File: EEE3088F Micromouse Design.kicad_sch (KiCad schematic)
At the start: 42 parts, among them J1 Conn_02x16_Odd_Even, J2 Conn_01x02, U1 INA219AxD, U2 DRV8837, U3 DRV8837, U4 DRV8837, U5 DRV8837, U6 TPS5430DDA, U7 TPS61088RHLR

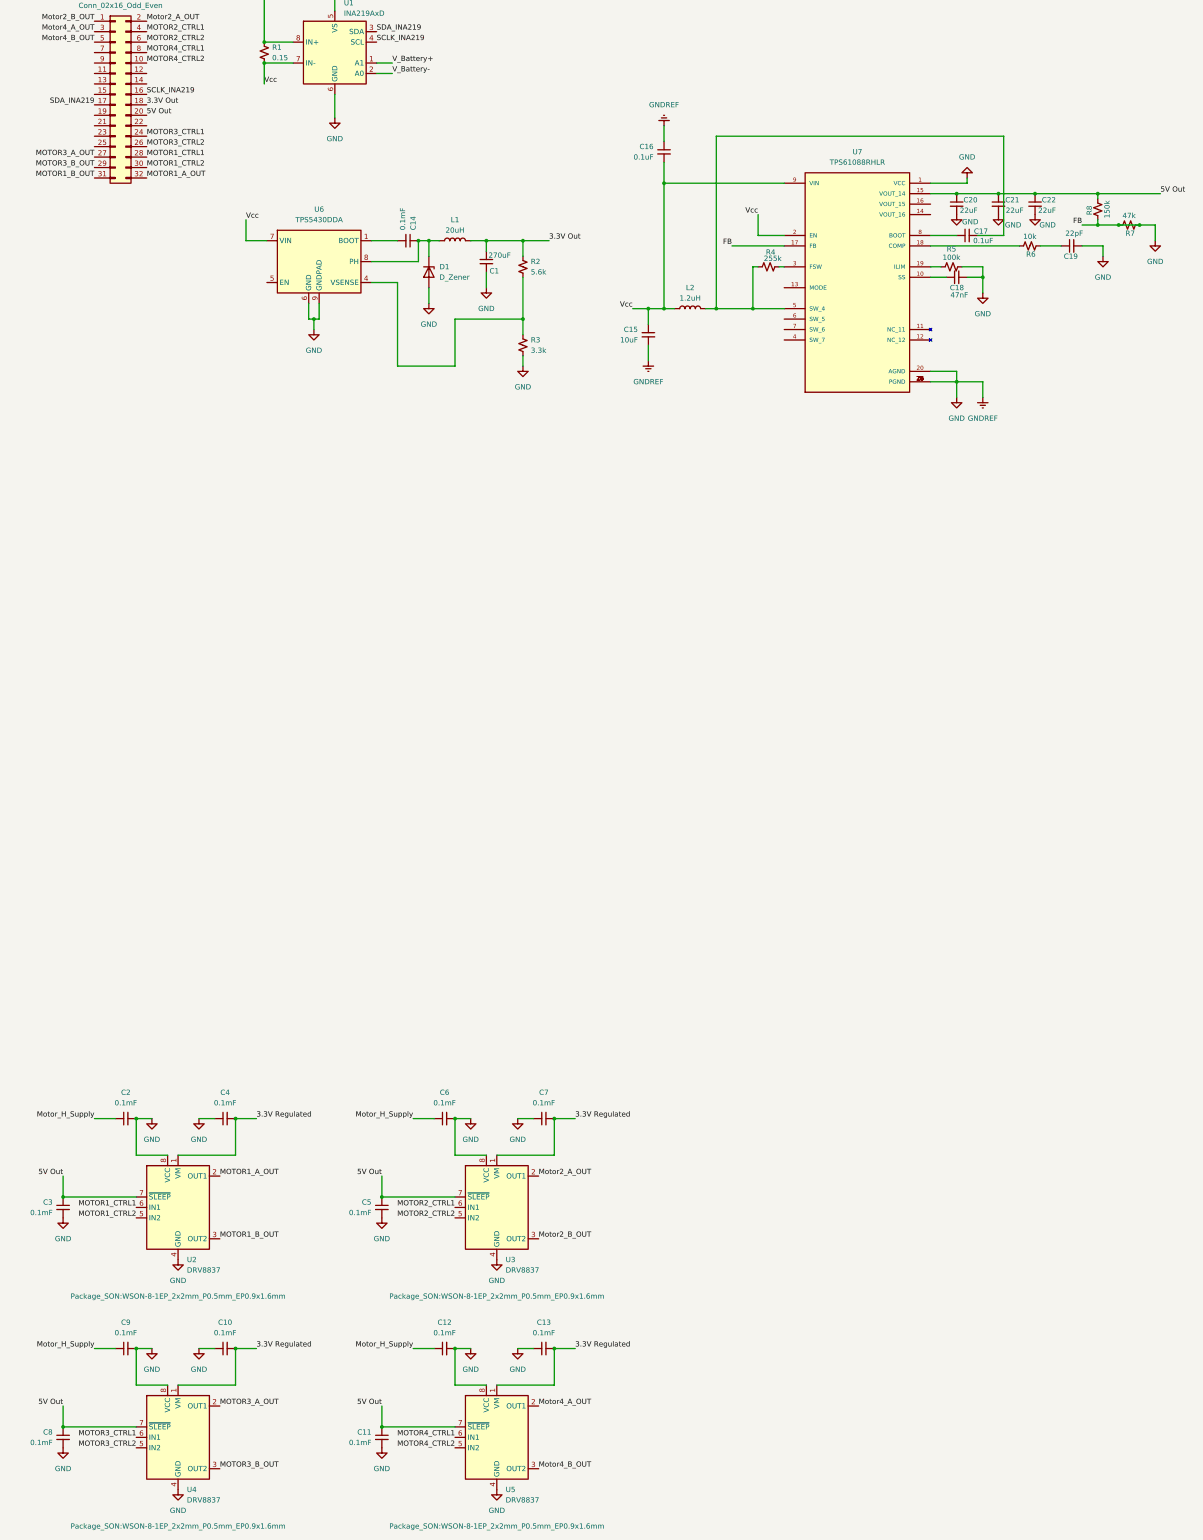
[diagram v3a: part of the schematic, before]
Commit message: Added the Battery Charging Circuit
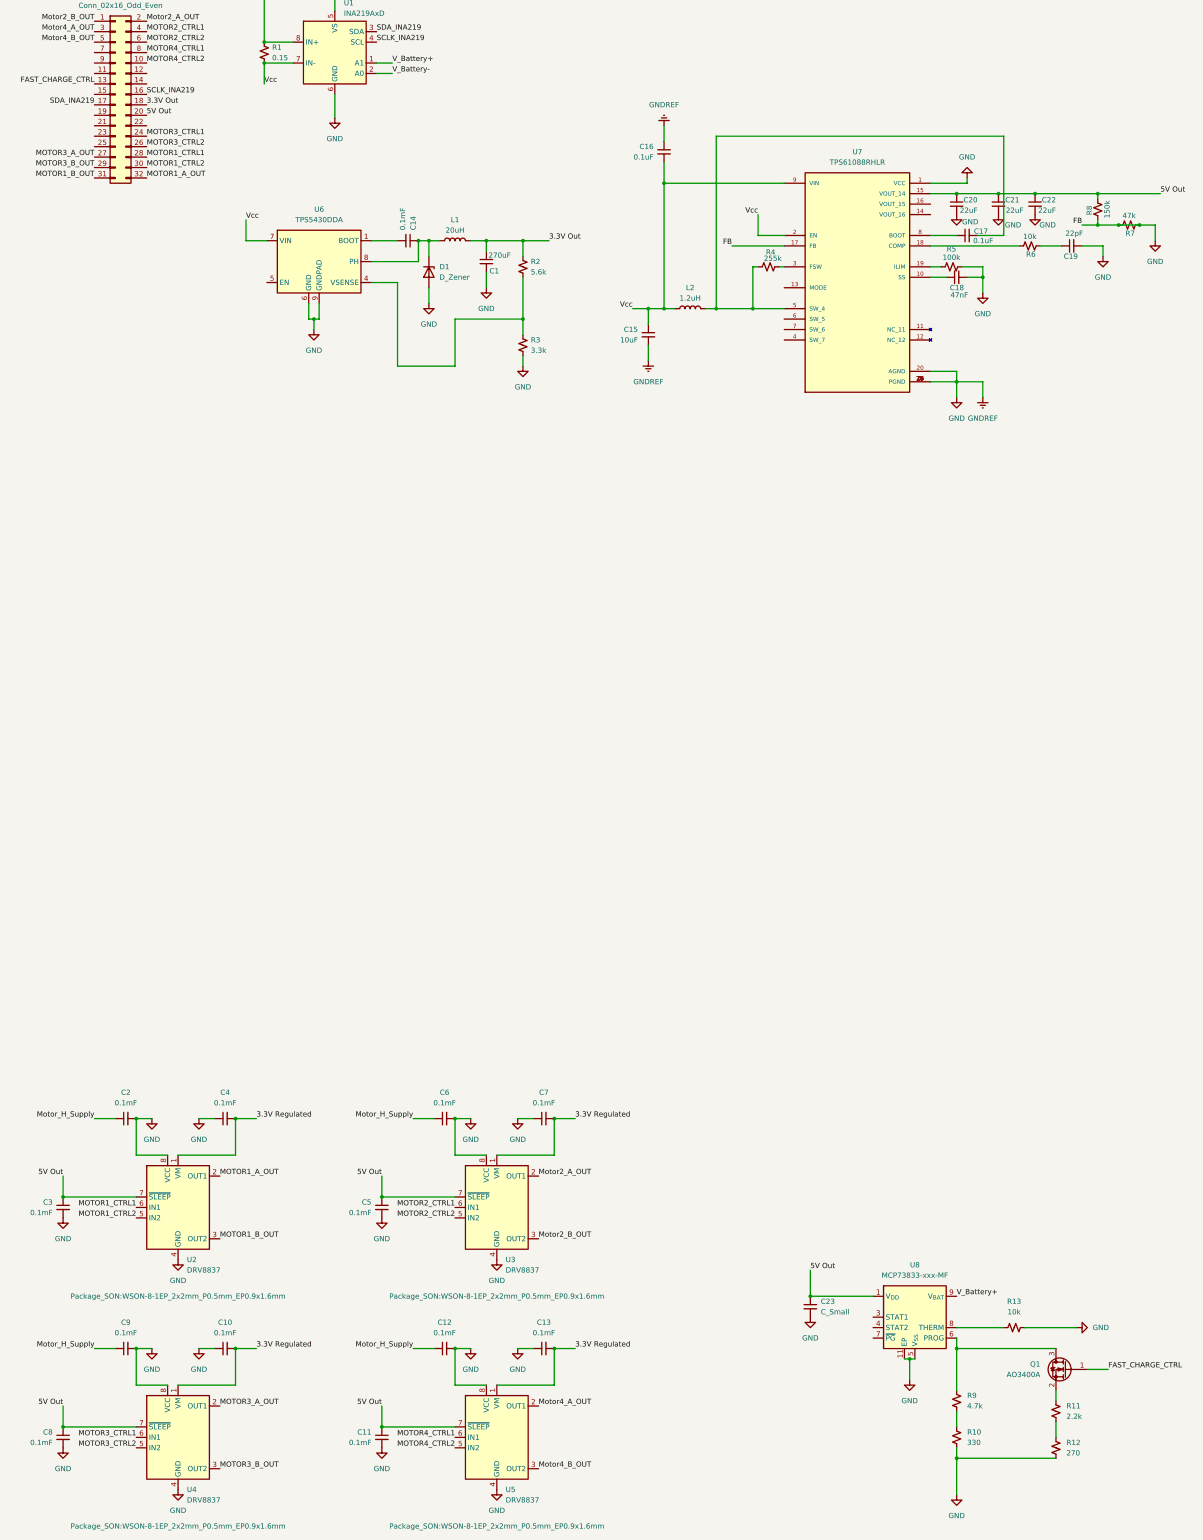
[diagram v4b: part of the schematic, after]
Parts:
- added C23: C_Small, symbol Device:C_Small
- added Q1: AO3400A, Package_TO_SOT_SMD:SOT-23, symbol Transistor_FET:AO3400A
- added R10: 330, Resistor_SMD:R_1206_3216Metric_Pad1.30x1.75mm_HandSolder, symbol Device:R_Small_US
- added R11: 2.2k, Resistor_SMD:R_1206_3216Metric_Pad1.30x1.75mm_HandSolder, symbol Device:R_Small_US
- added R12: 270, Resistor_SMD:R_1206_3216Metric_Pad1.30x1.75mm_HandSolder, symbol Device:R_Small_US
- added R13: 10k, Resistor_SMD:R_1206_3216Metric_Pad1.30x1.75mm_HandSolder, symbol Device:R_Small_US
- added R9: 4.7k, Resistor_SMD:R_1206_3216Metric_Pad1.30x1.75mm_HandSolder, symbol Device:R_Small_US
- added U8: MCP73833-xxx-MF, Package_DFN_QFN:DFN-10-1EP_3x3mm_P0.5mm_EP1.58x2.35mm, symbol Battery_Management:MCP73833-xxx-MF
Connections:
- net 5V Out: now also C23.1, U8.1 (V_{DD}), U8.2 (V_{DD})
- net GND: now also C23.2, R10.2, R12.2, R13.2, U8.11 (EP), U8.5 (V_{SS})
- net V_Battery+: now also U8.10 (V_{BAT}), U8.9 (V_{BAT})
- net FAST_CHARGE_CTRL: now reaches J1.13 (Pin_13)
- net FAST_CHARGE_CTRL: now also Q1.1 (G)
- new net: Q1.3 (D), R9.1, U8.6 (PROG)
- new net: R13.1, U8.8 (THERM)
- new net: Q1.2 (S), R11.1
- new net: R10.1, R9.2
- new net: R11.2, R12.1

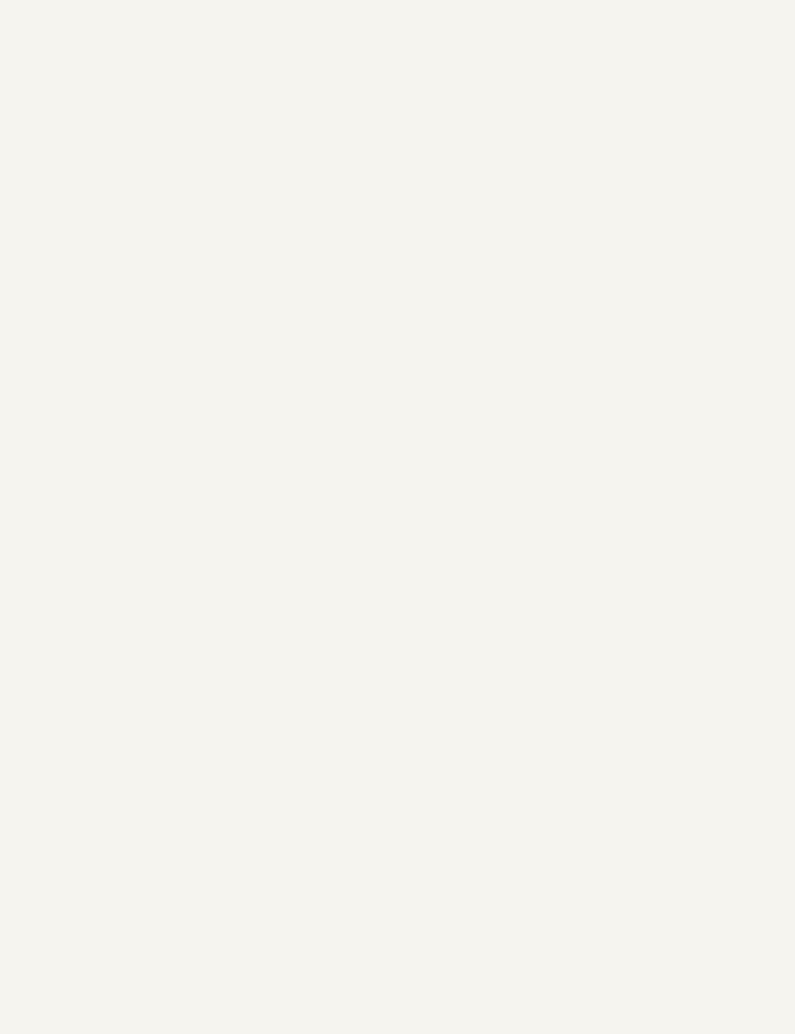
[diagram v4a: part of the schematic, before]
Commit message: Added Type-C 9V integration
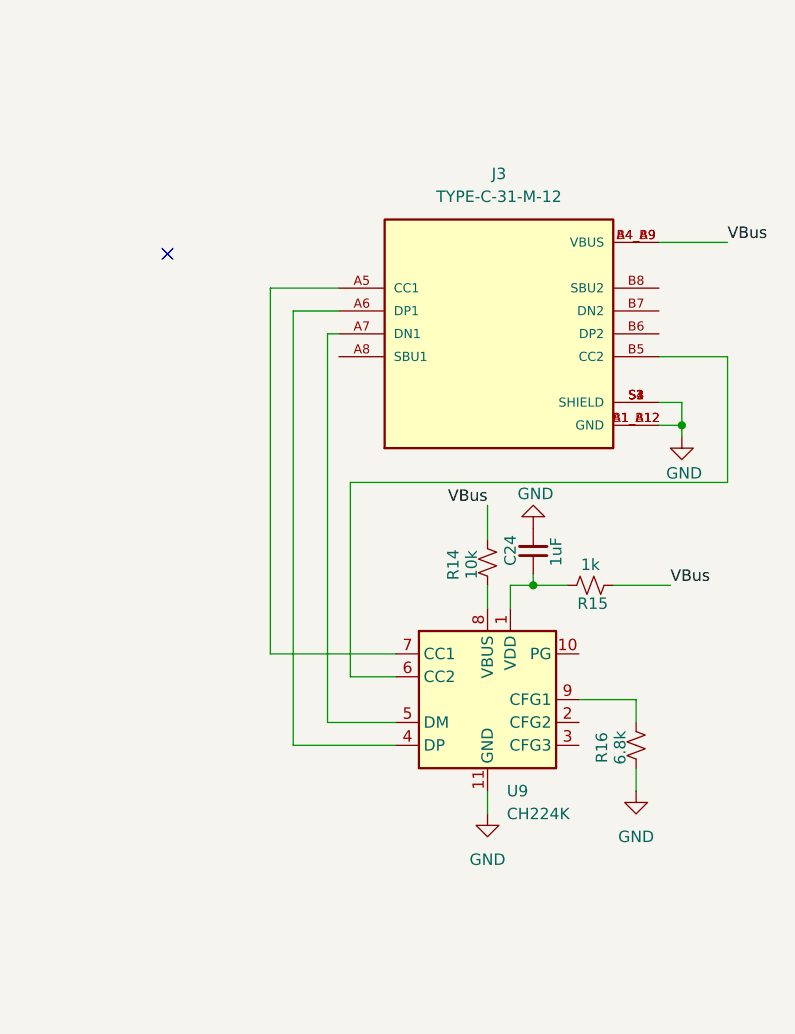
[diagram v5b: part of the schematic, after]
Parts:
- added C24: 1uF, Capacitor_SMD:C_0402_1005Metric_Pad0.74x0.62mm_HandSolder, symbol Device:C_Small
- added J3: TYPE-C-31-M-12, TYPE-C-31-M-12:HRO_TYPE-C-31-M-12, symbol TYPE-C-31-M-12:TYPE-C-31-M-12
- added R14: 10k, Resistor_SMD:R_1206_3216Metric_Pad1.30x1.75mm_HandSolder, symbol Device:R_Small_US
- added R15: 1k, Resistor_SMD:R_1206_3216Metric_Pad1.30x1.75mm_HandSolder, symbol Device:R_Small_US
- added R16: 6.8k, Resistor_SMD:R_1206_3216Metric_Pad1.30x1.75mm_HandSolder, symbol Device:R_Small_US
- added U9: CH224K, Package_SO:SSOP-10-1EP_3.9x4.9mm_P1mm_EP2.1x3.3mm, symbol Interface_USB:CH224K
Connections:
- net GND: now also C24.2, J3.A1_B12 (GND), J3.B1_A12 (GND), J3.S1 (SHIELD), J3.S2 (SHIELD), J3.S3 (SHIELD), J3.S4 (SHIELD), R16.1, U9.11 (GND)
- new net: R14.1, U9.8 (VBUS)
- new net: C24.1, R15.2, U9.1 (VDD)
- new net: J3.A5 (CC1), U9.7 (CC1)
- new net: J3.A6 (DP1), U9.4 (DP)
- new net: J3.A7 (DN1), U9.5 (DM)
- new net: J3.B5 (CC2), U9.6 (CC2)
- new net: R16.2, U9.9 (CFG1)
- new net VBus: J3.A4_B9 (VBUS), J3.B4_A9 (VBUS), R14.2, R15.1
- no-connect marks 0 -> 1

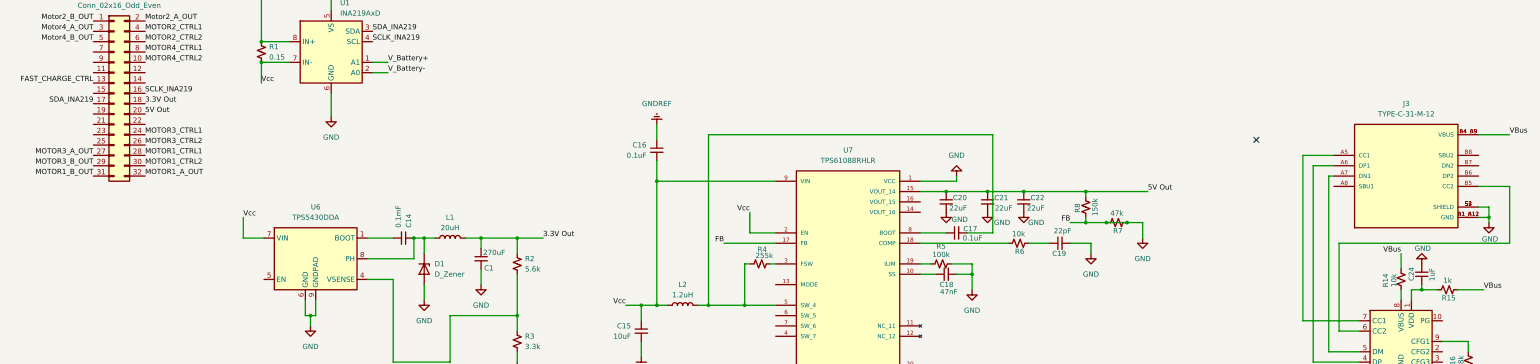
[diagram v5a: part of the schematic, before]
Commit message: Fixed some connector labels
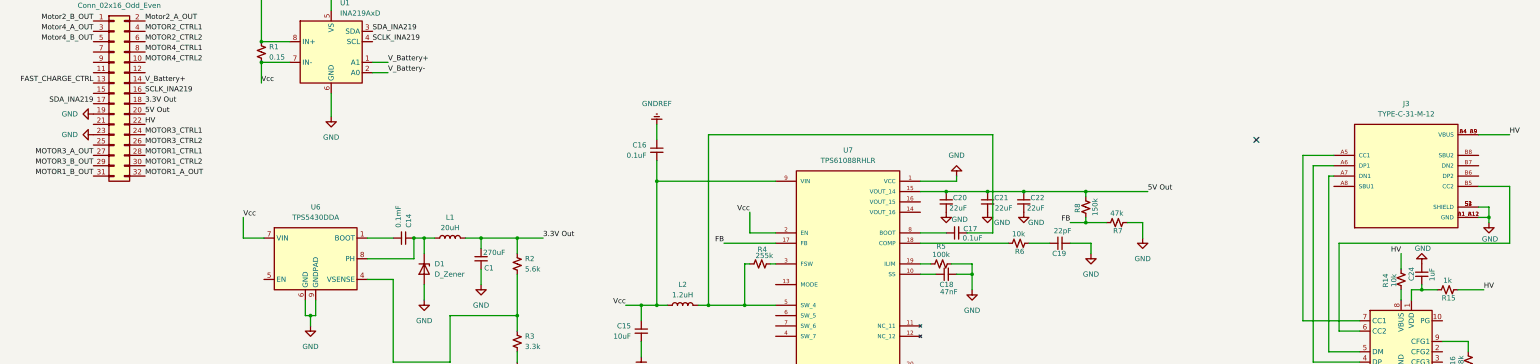
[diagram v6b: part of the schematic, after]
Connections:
- net VBus is gone; now on net HV: J3.A4_B9 (VBUS), J3.B4_A9 (VBUS), R14.2, R15.1
- net GND: now also J1.19 (Pin_19), J1.23 (Pin_23); no longer R7.2, R8.1, U7.17 (FB)
- net V_Battery+: now also J1.14 (Pin_14)
- net HV: now reaches J1.22 (Pin_22)
- new net FB: R7.2, R8.1, U7.17 (FB)
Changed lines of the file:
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@@
 	)
 	(junction
-		(at 285.75 86.36)
-		(diameter 0)
-		(color 0 0 0 0)
-	)
-	(junction
-		(at 280.67 86.36)
-		(diameter 0)
-		(color 0 0 0 0)
-	)
-	(junction
 		(at 260.35 78.74)
 		(diameter 0)
@@
 	(wire
 		(pts
-			(xy 285.75 86.36) (xy 280.67 86.36)
-		)
-		(stroke
-			(width 0)
-			(type default)
-		)
-	)
-	(wire
-		(pts
 			(xy 369.57 115.57) (xy 363.22 115.57)
 		)
@@
 		)
 	)
-	(label "VBus"
+	(label "HV"
 		(at 353.06 93.98 180)
 		(effects
@@
 		)
 	)
+	(label "HV"
+		(at 44.45 62.23 0)
+		(effects
+			(font
+				(size 1.27 1.27)
+			)
+			(justify left bottom)
+		)
+	)
 	(label "FB"
 		(at 186.69 91.44 180)
@@
 	)
 	(label "V_Battery+"
+		(at 44.45 52.07 0)
+		(effects
+			(font
+				(size 1.27 1.27)
+			)
+			(justify left bottom)
+		)
+	)
+	(label "V_Battery+"
 		(at 241.3 346.71 0)
 		(effects
@@
 		)
 	)
-	(label "VBus"
+	(label "HV"
 		(at 379.73 64.77 0)
 		(effects
@@
 		)
 	)
-	(label "VBus"
+	(label "HV"
 		(at 373.38 102.87 0)
 		(effects
@@
 	)
 	(symbol
+		(lib_id "power:GND")
+		(at 31.75 59.69 270)
+		(unit 1)
+		(exclude_from_sim no)
+		(in_bom yes)
+		(on_board yes)
+		(dnp no)
+		(fields_autoplaced yes)
+		(property "Reference" "#PWR041"
+			(at 25.4 59.69 0)
+			(effects
+				(font
+					(size 1.27 1.27)
+				)
+				(hide yes)
+			)
+		)
+		(property "Value" "GND"
+			(at 27.94 59.6899 90)
+			(effects
+				(font
+					(size 1.27 1.27)
+				)
+				(justify right)
+			)
+		)
+		(property "Footprint" ""
+			(at 31.75 59.69 0)
+			(effects
+				(font
+					(size 1.27 1.27)
+				)
+				(hide yes)
+			)
+		)
+		(property "Datasheet" ""
+			(at 31.75 59.69 0)
+			(effects
+				(font
+					(size 1.27 1.27)
+				)
+				(hide yes)
+			)
+		)
+		(property "Description" ""
+			(at 31.75 59.69 0)
+			(effects
+				(font
+					(size 1.27 1.27)
+				)
+			)
+		)
+		(pin "1"
+		)
+		(instances
+			(project "EEE3088F Micromouse Design"
+				(path "/9da86a77-c081-4eef-8f80-aa4f3cdcfcf8"
+					(reference "#PWR041")
+					(unit 1)
+				)
+			)
+		)
+	)
+	(symbol
 		(lib_id "Device:R_Small_US")
 		(at 255.27 354.33 90)
@@
 					(unit 1)
 				)
+			)
+		)
+	)
+	(symbol
+		(lib_id "power:GND")
+		(at 31.75 64.77 270)
+		(unit 1)
+		(exclude_from_sim no)
+		(in_bom yes)
+		(on_board yes)
+		(dnp no)
+		(fields_autoplaced yes)
+		(property "Reference" "#PWR042"
+			(at 25.4 64.77 0)
+			(effects
+				(font
+					(size 1.27 1.27)
+				)
+				(hide yes)
+			)
+		)
+		(property "Value" "GND"
+			(at 27.94 64.7699 90)
+			(effects
+				(font
+					(size 1.27 1.27)
+				)
+				(justify right)
+			)
+		)
+		(property "Footprint" ""
+			(at 31.75 64.77 0)
+			(effects
+				(font
+					(size 1.27 1.27)
+				)
+				(hide yes)
+			)
+		)
+		(property "Datasheet" ""
+			(at 31.75 64.77 0)
+			(effects
+				(font
+					(size 1.27 1.27)
+				)
+				(hide yes)
+			)
+		)
+		(property "Description" ""
+			(at 31.75 64.77 0)
+			(effects
+				(font
+					(size 1.27 1.27)
+				)
+			)
+		)
+		(pin "1"
+		)
+		(instances
+			(project "EEE3088F Micromouse Design"
+				(path "/9da86a77-c081-4eef-8f80-aa4f3cdcfcf8"
+					(reference "#PWR042")
+					(unit 1)
+				)

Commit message: Redid the Motor circuit with an Improved IC
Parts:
- added C25: 1uF, symbol Device:C_Small
- added C26: 22pF, symbol Device:C_Small
- added C27, C28, C31, C32: 2.2uF, symbol Device:C_Small
- added C29, C30: 10uF, symbol Device:C_Small
- added R17: 87k, Resistor_SMD:R_1206_3216Metric_Pad1.30x1.75mm_HandSolder, symbol Device:R_Small_US
- added R18, R21, R22: 13k, Resistor_SMD:R_1206_3216Metric_Pad1.30x1.75mm_HandSolder, symbol Device:R_Small_US
- added R19, R20: 700, Resistor_SMD:R_1206_3216Metric_Pad1.30x1.75mm_HandSolder, symbol Device:R_Small_US
- added R23, R24: 100, Resistor_SMD:R_1206_3216Metric_Pad1.30x1.75mm_HandSolder, symbol Device:R_Small_US
- added R25, R26, R27, R28: 1, Resistor_SMD:R_1206_3216Metric_Pad1.30x1.75mm_HandSolder, symbol Device:R_Small_US
- added U10: BQ24650, Package_DFN_QFN:Texas_RVA_VQFN-16-1EP_3.5x3.5mm_P0.5mm_EP2.14x2.14mm_ThermalVias, symbol Battery_Management:BQ24650
- added U11, U12: DRV8833PW, Package_SO:TSSOP-16_4.4x5mm_P0.65mm, symbol Driver_Motor:DRV8833PW
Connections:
- net 5V Out: no longer C23.1, U8.1 (V_{DD}), U8.2 (V_{DD})
- net GND: now also C25.2, C27.1, C29.1, C30.1, C32.1, R18.2, R21.2, R24.2, R25.2, R26.2, R27.2, R28.2, U11.13 (GND), U12.13 (GND)
- net HV: now also R17.1, R22.1, U10.1 (VCC)
- net MOTOR1_A_OUT: now also U11.2 (AOUT1)
- net MOTOR1_B_OUT: now also U11.4 (AOUT2)
- net MOTOR1_CTRL1: now also U11.16 (AIN1)
- net MOTOR1_CTRL2: now also U11.15 (AIN2)
- net MOTOR2_CTRL1: now also U11.9 (BIN1)
- net MOTOR2_CTRL2: now also U11.10 (BIN2)
- net MOTOR3_A_OUT: now also U12.2 (AOUT1)
- net MOTOR3_B_OUT: now also U12.4 (AOUT2)
- net MOTOR3_CTRL1: now also U12.16 (AIN1)
- net MOTOR3_CTRL2: now also U12.15 (AIN2)
- net MOTOR4_CTRL1: now also U12.9 (BIN1)
- net MOTOR4_CTRL2: now also U12.10 (BIN2)
- net Motor2_A_OUT: now also U11.7 (BOUT1)
- net Motor2_B_OUT: now also U11.5 (BOUT2)
- net Motor4_A_OUT: now also U12.7 (BOUT1)
- net Motor4_B_OUT: now also U12.5 (BOUT2)
- net V_Battery+: now also C26.2, R23.1
- net 3.3V Out renamed 3V3 Out
- net 3V3 Out: now also C25.1, U10.6 (VREF), U10.7 (TERM_EN)
- new net: R17.2, R18.1, U10.2 (MPPSET)
- new net: R27.1, U12.6 (BISEN)
- new net: R21.1, R22.2, U8.1 (V_{DD}), U8.2 (V_{DD})
- new net: C26.1, R23.2, R24.1, U10.8 (VFB)
- new net: C30.2, C31.1, U12.12 (VM)
- new net: C28.1, C29.2, U11.12 (VM)
- new net: R20.1, U10.5 (STAT2)
- new net: R25.1, U11.3 (AISEN)
- new net: C31.2, U12.11 (VCP)
- new net: R28.1, U12.3 (AISEN)
- new net: C32.2, U12.14 (VINT)
- new net: C28.2, U11.11 (VCP)
- new net: C27.2, U11.14 (VINT)
- new net: R26.1, U11.6 (BISEN)
- new net: R19.1, U10.3 (STAT1)
- new net: U10.11 (GND), U10.17 (GND)
- new net find LED: R19.2, R20.2
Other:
- note added: "GRAVEYARD OF DESIGNS (Remove When Populating Footprints)"
- moved on the sheet: C10, C11, C12, C13, C2, C23, C3, C4, C5, C6, C7, C8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
